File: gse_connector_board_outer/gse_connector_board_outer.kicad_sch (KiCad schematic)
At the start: 8 parts, among them J1 arming_connector, J2 gse_com_connector, J3 chg_connector, J5 Conn_02x02_Top_Bottom, J6 Conn_02x02_Top_Bottom, J7 Conn_02x02_Top_Bottom

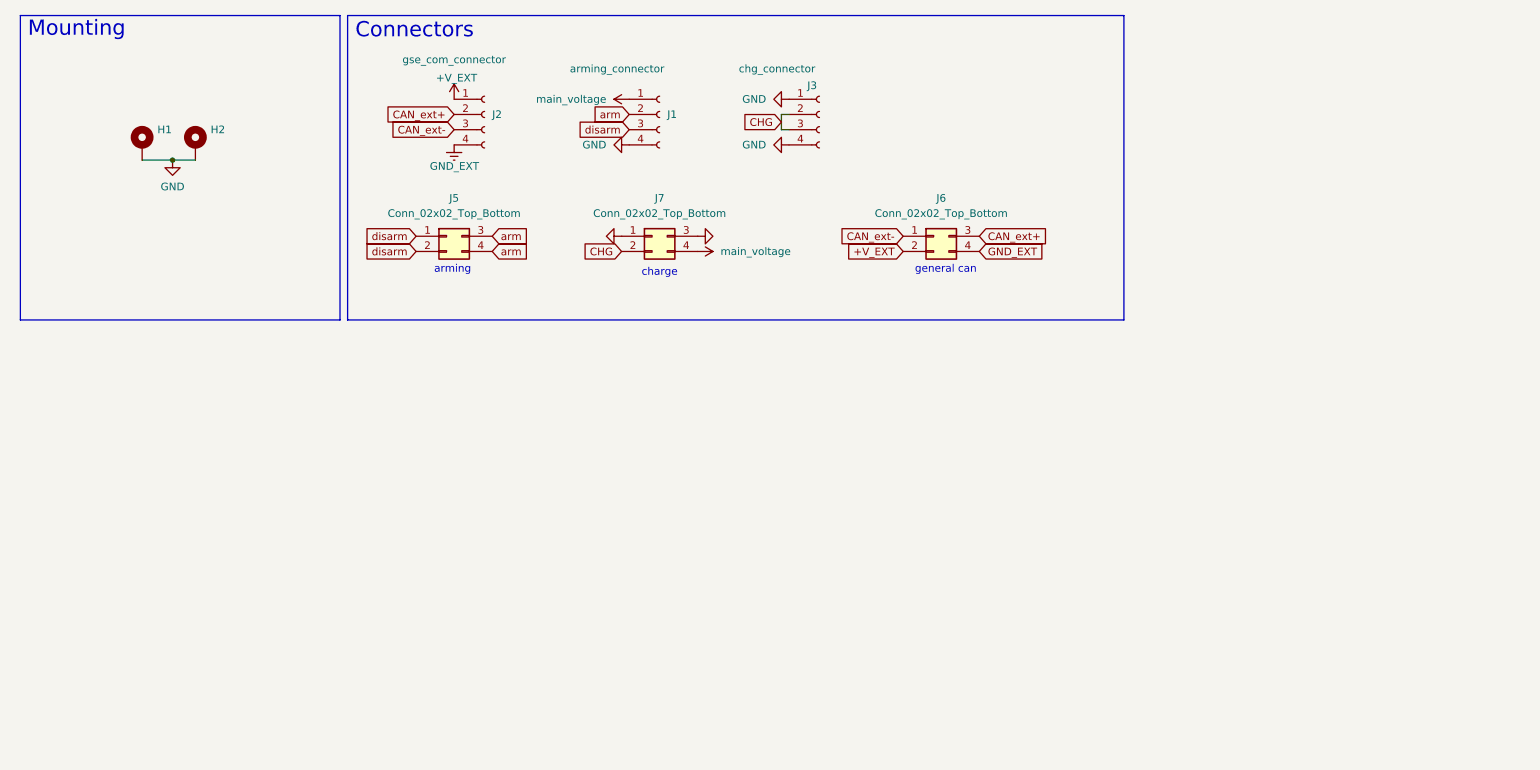
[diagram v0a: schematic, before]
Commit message: changed the footprints of the magnetic connector and routing of inner board
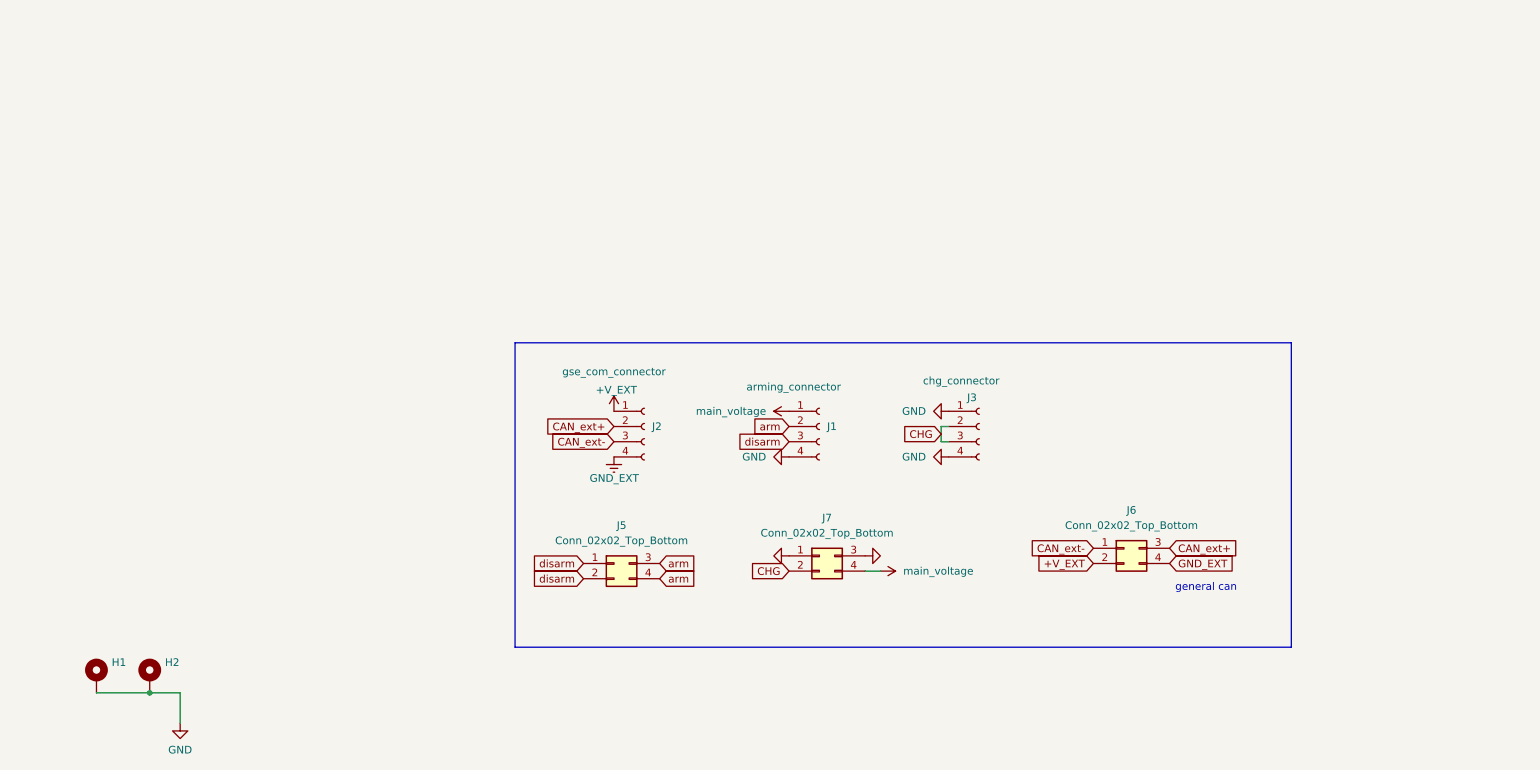
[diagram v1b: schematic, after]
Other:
- note removed: "Connectors"
- note removed: "Mounting"
- note removed: "arming"
- note removed: "charge"
- title: GSE connector outer -> (none)
- moved on the sheet: H1, H2, J1, J2, J3, J5, J6, J7

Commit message: implemented changes
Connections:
- net CHG: now also J7.3 (Pin_3), J7.4 (Pin_4); no longer J7.2 (Pin_2)
- net GND: now also J7.2 (Pin_2); no longer J1.4 (Pin_4), J7.3 (Pin_3)
- net arm: no longer J5.3 (Pin_3)
- net disarm: no longer J5.1 (Pin_1)
- net main_voltage renamed Voltage_Arm
- net Voltage_Arm: now also J5.3 (Pin_3); no longer J7.4 (Pin_4)
- new net GND_Arm: J1.4 (Pin_4), J5.1 (Pin_1)
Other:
- moved on the sheet: J1, J2, J3, J5, J7

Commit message: cleanup silkscreen
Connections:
- net arm: now also J5.2 (Pin_2); no longer J5.4 (Pin_4)
- net disarm: now also J5.4 (Pin_4); no longer J5.2 (Pin_2)
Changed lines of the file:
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@@
 	(global_label "disarm"
 		(shape input)
-		(at 113.03 107.95 180)
+		(at 125.73 107.95 0)
 		(fields_autoplaced yes)
 		(effects
@@
 				(size 1.27 1.27)
 			)
-			(justify right)
+			(justify left)
 		)
 		(property "Intersheetrefs" "${INTERSHEET_REFS}"
-			(at 103.6344 107.95 0)
+			(at 135.1256 107.95 0)
 			(hide yes)
 			(show_name no)
@@
 					(size 1.27 1.27)
 				)
-				(justify right)
+				(justify left)
 			)
 		)
@@
 	(global_label "arm"
 		(shape input)
-		(at 125.73 107.95 0)
+		(at 113.03 107.95 180)
 		(fields_autoplaced yes)
 		(effects
@@
 				(size 1.27 1.27)
 			)
-			(justify left)
+			(justify right)
 		)
 		(property "Intersheetrefs" "${INTERSHEET_REFS}"
-			(at 132.3437 107.95 0)
+			(at 106.4163 107.95 0)
 			(hide yes)
 			(show_name no)
@@
 					(size 1.27 1.27)
 				)
-				(justify left)
+				(justify right)
 			)
 		)

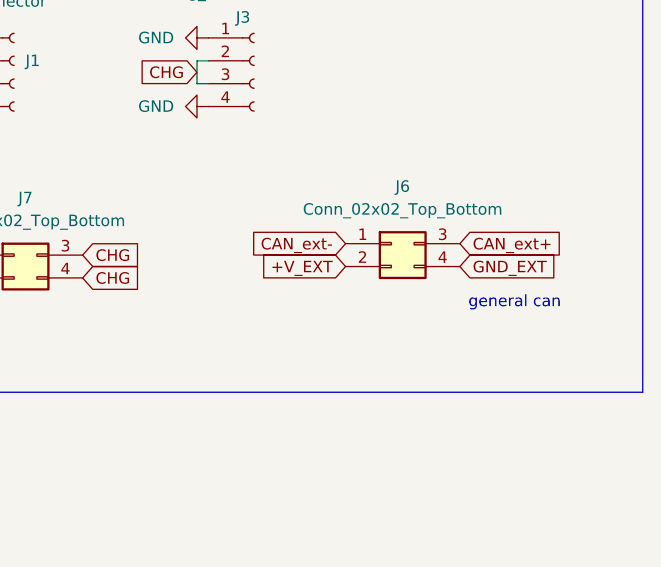
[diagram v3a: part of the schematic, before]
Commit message: fix connector pinout
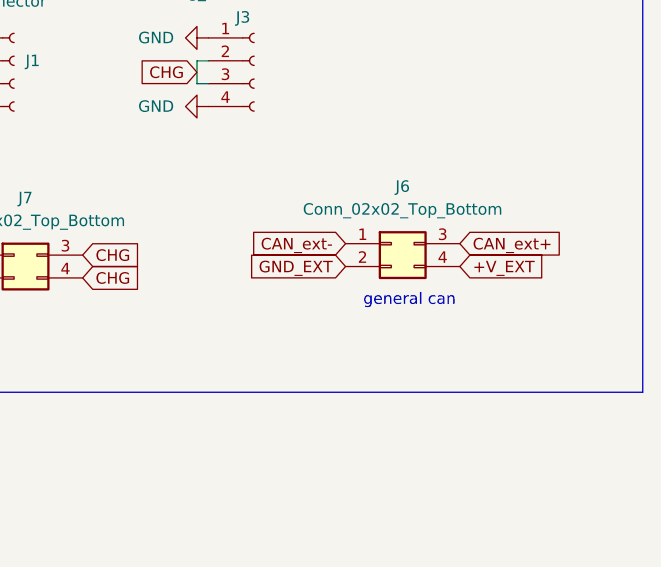
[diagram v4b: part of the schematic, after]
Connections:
- net +V_EXT: now also J6.4 (Pin_4); no longer J6.2 (Pin_2)
- net GND_EXT: now also J6.2 (Pin_2); no longer J6.4 (Pin_4)
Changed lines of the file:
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@@
 	(text "general can"
 		(exclude_from_sim no)
-		(at 210.566 109.474 0)
+		(at 198.882 109.22 0)
 		(effects
 			(font
@@
 	(global_label "+V_EXT"
 		(shape input)
+		(at 204.47 105.41 0)
+		(fields_autoplaced yes)
+		(effects
+			(font
+				(size 1.27 1.27)
+			)
+			(justify left)
+		)
+		(property "Intersheetrefs" "${INTERSHEET_REFS}"
+			(at 214.4099 105.41 0)
+			(hide yes)
+			(show_name no)
+			(do_not_autoplace no)
+			(effects
+				(font
+					(size 1.27 1.27)
+				)
+				(justify left)
+			)
+		)
+	)
+	(global_label "arm"
+		(shape input)
+		(at 149.86 82.55 180)
+		(fields_autoplaced yes)
+		(effects
+			(font
+				(size 1.27 1.27)
+			)
+			(justify right)
+		)
+		(property "Intersheetrefs" "${INTERSHEET_REFS}"
+			(at 143.2463 82.55 0)
+			(hide yes)
+			(show_name no)
+			(do_not_autoplace no)
+			(effects
+				(font
+					(size 1.27 1.27)
+				)
+				(justify right)
+			)
+		)
+	)
+	(global_label "CHG"
+		(shape input)
+		(at 175.26 83.82 180)
+		(fields_autoplaced yes)
+		(effects
+			(font
+				(size 1.27 1.27)
+			)
+			(justify right)
+		)
+		(property "Intersheetrefs" "${INTERSHEET_REFS}"
+			(at 168.4043 83.82 0)
+			(hide yes)
+			(show_name no)
+			(do_not_autoplace no)
+			(effects
+				(font
+					(size 1.27 1.27)
+				)
+				(justify right)
+			)
+		)
+	)
+	(global_label "CAN_ext-"
+		(shape input)
+		(at 191.77 102.87 180)
+		(fields_autoplaced yes)
+		(effects
+			(font
+				(size 1.27 1.27)
+			)
+			(justify right)
+		)
+		(property "Intersheetrefs" "${INTERSHEET_REFS}"
+			(at 179.7133 102.87 0)
+			(hide yes)
+			(show_name no)
+			(do_not_autoplace no)
+			(effects
+				(font
+					(size 1.27 1.27)
+				)
+				(justify right)
+			)
+		)
+	)
+	(global_label "CAN_ext-"
+		(shape input)
+		(at 118.11 85.09 180)
+		(fields_autoplaced yes)
+		(effects
+			(font
+				(size 1.27 1.27)
+			)
+			(justify right)
+		)
+		(property "Intersheetrefs" "${INTERSHEET_REFS}"
+			(at 106.0533 85.09 0)
+			(hide yes)
+			(show_name no)
+			(do_not_autoplace no)
+			(effects
+				(font
+					(size 1.27 1.27)
+				)
+				(justify right)
+			)
+		)
+	)
+	(global_label "disarm"
+		(shape input)
+		(at 125.73 107.95 0)
+		(fields_autoplaced yes)
+		(effects
+			(font
+				(size 1.27 1.27)
+			)
+			(justify left)
+		)
+		(property "Intersheetrefs" "${INTERSHEET_REFS}"
+			(at 135.1256 107.95 0)
+			(hide yes)
+			(show_name no)
+			(do_not_autoplace no)
+			(effects
+				(font
+					(size 1.27 1.27)
+				)
+				(justify left)
+			)
+		)
+	)
+	(global_label "CHG"
+		(shape input)
+		(at 162.56 104.14 0)
+		(fields_autoplaced yes)
+		(effects
+			(font
+				(size 1.27 1.27)
+			)
+			(justify left)
+		)
+		(property "Intersheetrefs" "${INTERSHEET_REFS}"
+			(at 169.4157 104.14 0)
+			(hide yes)
+			(show_name no)
+			(do_not_autoplace no)
+			(effects
+				(font
+					(size 1.27 1.27)
+				)
+				(justify left)
+			)
+		)
+	)
+	(global_label "GND_EXT"
+		(shape input)
 		(at 191.77 105.41 180)
 		(fields_autoplaced yes)
@@
 		)
 		(property "Intersheetrefs" "${INTERSHEET_REFS}"
-			(at 181.8301 105.41 0)
-			(hide yes)
-			(show_name no)
-			(do_not_autoplace no)
-			(effects
-				(font
-					(size 1.27 1.27)
-				)
-				(justify right)
-			)
-		)
-	)
-	(global_label "arm"
-		(shape input)
-		(at 149.86 82.55 180)
-		(fields_autoplaced yes)
-		(effects
-			(font
-				(size 1.27 1.27)
-			)
-			(justify right)
-		)
-		(property "Intersheetrefs" "${INTERSHEET_REFS}"
-			(at 143.2463 82.55 0)
-			(hide yes)
-			(show_name no)
-			(do_not_autoplace no)
-			(effects
-				(font
-					(size 1.27 1.27)
-				)
-				(justify right)
-			)
-		)
-	)
-	(global_label "CHG"
-		(shape input)
-		(at 175.26 83.82 180)
-		(fields_autoplaced yes)
-		(effects
-			(font
-				(size 1.27 1.27)
-			)
-			(justify right)
-		)
-		(property "Intersheetrefs" "${INTERSHEET_REFS}"
-			(at 168.4043 83.82 0)
-			(hide yes)
-			(show_name no)
-			(do_not_autoplace no)
-			(effects
-				(font
-					(size 1.27 1.27)
-				)
-				(justify right)
-			)
-		)
-	)
-	(global_label "CAN_ext-"
-		(shape input)
-		(at 191.77 102.87 180)
-		(fields_autoplaced yes)
-		(effects
-			(font
-				(size 1.27 1.27)
-			)
-			(justify right)
-		)
-		(property "Intersheetrefs" "${INTERSHEET_REFS}"
-			(at 179.7133 102.87 0)
-			(hide yes)
-			(show_name no)
-			(do_not_autoplace no)
-			(effects
-				(font
-					(size 1.27 1.27)
-				)
-				(justify right)
-			)
-		)
-	)
-	(global_label "CAN_ext-"
-		(shape input)
-		(at 118.11 85.09 180)
-		(fields_autoplaced yes)
-		(effects
-			(font
-				(size 1.27 1.27)
-			)
-			(justify right)
-		)
-		(property "Intersheetrefs" "${INTERSHEET_REFS}"
-			(at 106.0533 85.09 0)
-			(hide yes)
-			(show_name no)
-			(do_not_autoplace no)
-			(effects
-				(font
-					(size 1.27 1.27)
-				)
-				(justify right)
-			)
-		)
-	)
-	(global_label "disarm"
-		(shape input)
-		(at 125.73 107.95 0)
-		(fields_autoplaced yes)
-		(effects
-			(font
-				(size 1.27 1.27)
-			)
-			(justify left)
-		)
-		(property "Intersheetrefs" "${INTERSHEET_REFS}"
-			(at 135.1256 107.95 0)
-			(hide yes)
-			(show_name no)
-			(do_not_autoplace no)
-			(effects
-				(font
-					(size 1.27 1.27)
-				)
-				(justify left)
-			)
-		)
-	)
-	(global_label "CHG"
-		(shape input)
-		(at 162.56 104.14 0)
-		(fields_autoplaced yes)
-		(effects
-			(font
-				(size 1.27 1.27)
-			)
-			(justify left)
-		)
-		(property "Intersheetrefs" "${INTERSHEET_REFS}"
-			(at 169.4157 104.14 0)
-			(hide yes)
-			(show_name no)
-			(do_not_autoplace no)
-			(effects
-				(font
-					(size 1.27 1.27)
-				)
-				(justify left)
-			)
-		)
-	)
-	(global_label "GND_EXT"
-		(shape input)
-		(at 204.47 105.41 0)
-		(fields_autoplaced yes)
-		(effects
-			(font
-				(size 1.27 1.27)
-			)
-			(justify left)
-		)
-		(property "Intersheetrefs" "${INTERSHEET_REFS}"
-			(at 215.6194 105.41 0)
-			(hide yes)
-			(show_name no)
-			(do_not_autoplace no)
-			(effects
-				(font
-					(size 1.27 1.27)
-				)
-				(justify left)
-			)
-		)
+			(at 180.6206 105.41 0)
+			(hide yes)
+			(show_name no)
+			(do_not_autoplace no)
+			(effects
+				(font
+					(size 1.27 1.27)
+				)
+				(justify right)
+			)
+		)

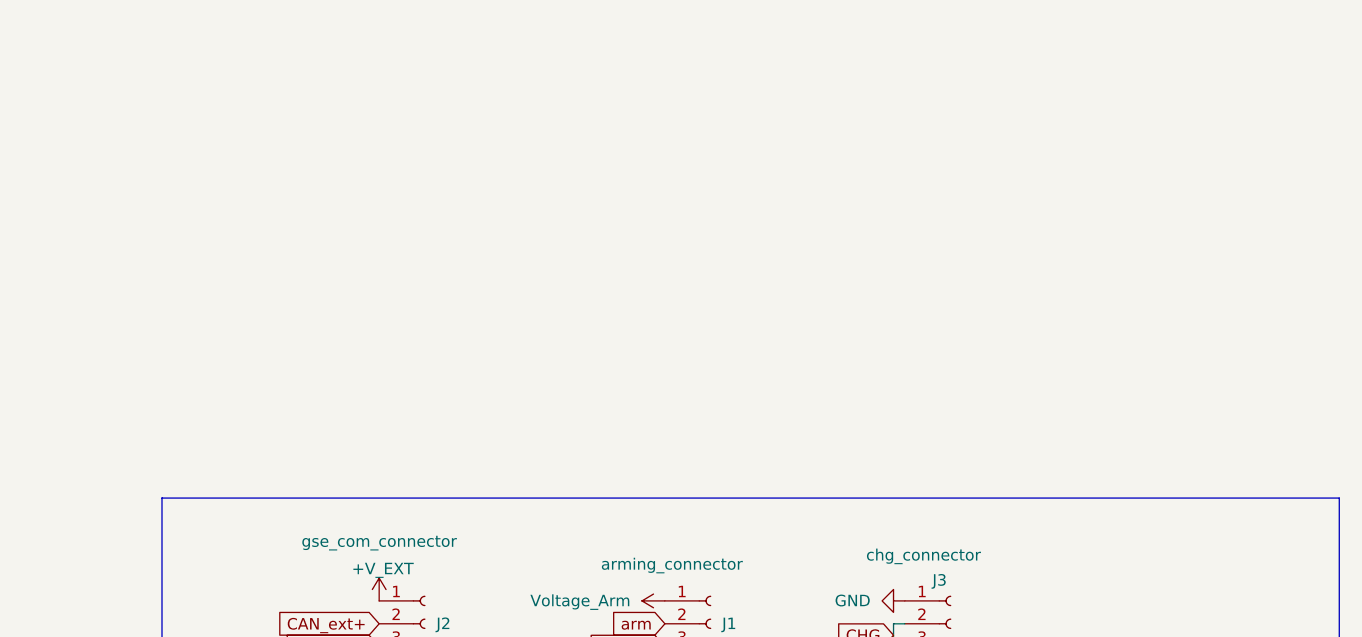
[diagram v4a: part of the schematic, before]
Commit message: replace can isolation with würth part
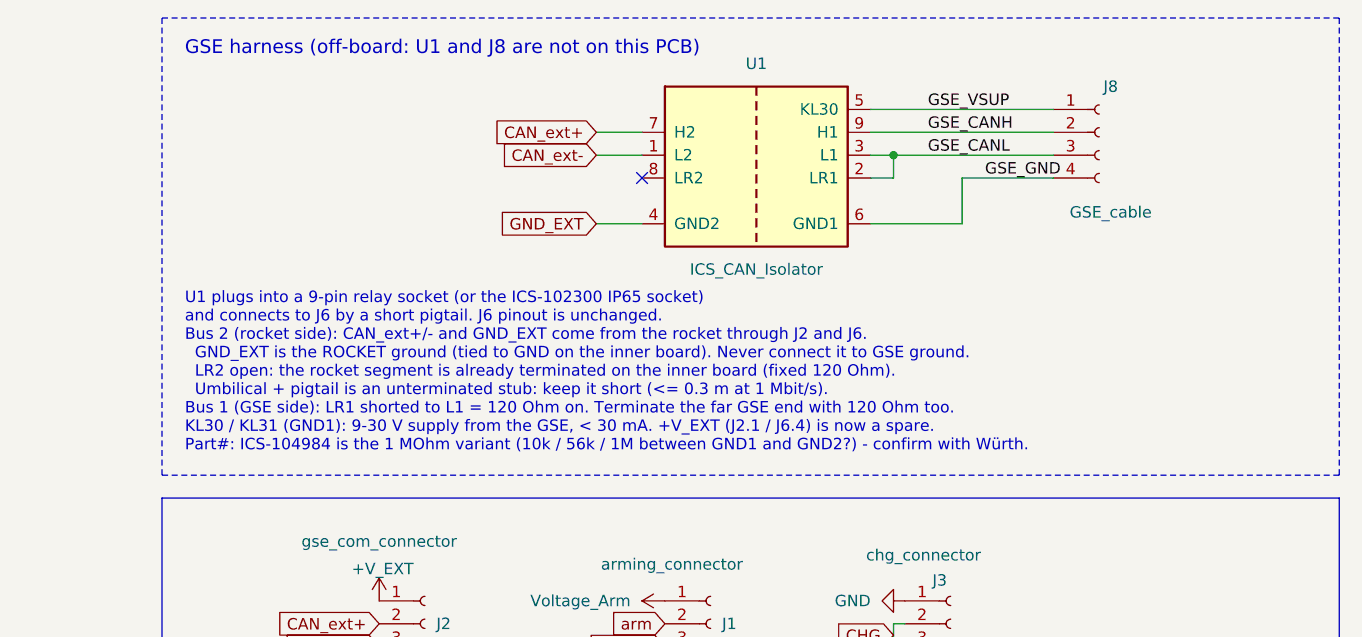
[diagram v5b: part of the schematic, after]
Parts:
- added J8: GSE_cable, symbol Connector:Conn_01x04_Socket
- added U1: ICS_CAN_Isolator, symbol custom_parts:ICS_CAN_Isolator
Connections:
- net CAN_ext+: now also U1.7 (H2)
- net CAN_ext-: now also U1.1 (L2)
- net GND_EXT: now also U1.4 (GND2)
- new net GSE_CANH: J8.2 (Pin_2), U1.9 (H1)
- new net GSE_CANL: J8.3 (Pin_3), U1.2 (LR1), U1.3 (L1)
- new net GSE_GND: J8.4 (Pin_4), U1.6 (GND1)
- new net GSE_VSUP: J8.1 (Pin_1), U1.5 (KL30)
- no-connect marks 0 -> 1
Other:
- note added: "GSE harness (off-board: U1 and J8 are not on this PCB)"
- note added: "U1 plugs into a 9-pin relay socket (or the ICS-102300 IP65 socket) and connects to J6 by a short pigtail. J6 pinout is unchanged. Bus 2 (rocket side): CAN_ext+/- and GND_EXT come from the rocket through J2 and J6. GND_EXT is the ROCKET ground (tied to GND on the inner board). Never connect it to GSE ground. LR2 open: the rocket segment is already terminated on the inner board (fixed 120 Ohm). Umb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"
